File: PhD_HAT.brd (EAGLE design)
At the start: 62.2 x 64.4 mm, 31 parts, among them J1 USB_MINI-B_SMT, J2 AVR_SPI_PROG_3X2PTH, J3 PJ-102AH/BH, Q2 2.5A/30V/105mΩ, U1 ATMEGA328P-MUR, U2 FT231XS, U3 3.3V

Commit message: Checkin- version
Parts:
- removed C1: 0.1uF, SparkFun-Capacitors:0603
- removed R1, R2: 4.7k, SparkFun-Resistors:0603
- removed U$1: SPARKFUN-CONNECTORS_RIGHT_ANGLED_DC, AG54_E_series_v2.29:SPARKFUN-CONNECTORS_M8_RIGHT_ANGLE_CONN
- added SJ1, SJ2: (no value), Adafruit Crickit FeatherWing:MICROBUILDER_SOLDERJUMPER_REFLOW
- added U$2: RPI-ZERO, RPI-Zero:RASPBERRYPI_BASTELSTUBE_V13_RASPI_BOARD_B+_FULL
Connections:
- removed net SCL: R1.1, U$1.P$2, U1.28
- removed net SDA: R2.1, U$1.P$3, U1.27
- new net N$10: SJ1.2
- new net N$7: SJ1.1, U2.4
- new net N$8: SJ2.1, U2.20
- net 3.3V: no longer C1.1, R1.2, R2.2, U$1.P$1
- net GND: no longer C1.2, U$1.P$4
- net RX: now also SJ2.2; no longer U2.20
- net TX: no longer U2.4
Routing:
- net SDA: track 59.2 -> 0.00 mm, vias 1 -> 0
- net 3.3V: track 102.5 -> 56.1 mm, vias 6 -> 5
- net SCL: track 26.5 -> 0.00 mm
- net RX: track 65.4 -> 56.6 mm

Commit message: Check-in of design files
A partial check-in to switch laptops
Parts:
- removed H1, H2, H3, H4: MOUNT-HOLE3.0, holes:3,0
- removed U$2: RPI-ZERO, RPI-Zero:RASPBERRYPI_BASTELSTUBE_V13_RASPI_BOARD_B+_FULL
- added C1: 1.0uF, SparkFun-Capacitors:0603
- added C9: 10uF, SparkFun-Capacitors:EIA3216
- added J4: (no value), SparkFun-Connectors:SCREWTERMINAL-3.5MM-5
- added J5: (no value), SparkFun-Connectors:SCREWTERMINAL-3.5MM-2
- added J6: (no value), SparkFun-Connectors:SCREWTERMINAL-3.5MM-4
- added SJ3, SJ4: (no value), Adafruit Crickit FeatherWing:MICROBUILDER_SOLDERJUMPER_ARROW_NOPASTE
- added U4: MIC39100-5.0WS, MIC39100-5.0WS:SOT223
- added X1: RASPI_BOARD_B+_H, raspberrypi_bastelstube_v13:RASPI_BOARD_B+HAT
- moved J3 17.8 mm to (10.2, 14.0)
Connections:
- removed net N$10: SJ1.2
- new net 3V3: X1.1
- new net 5V: C9.+, J6.1, U4.3
- new net 5V0: X1.2
- new net CLOCK: J6.3, U1.10
- new net DATA: J6.4, U1.11
- new net LATCH: J6.2, U1.9
- new net N$11: SJ3.1, X1.8
- new net N$12: SJ4.1, X1.10
- net GND: now also C1.2, C9.-, J5.1, J5.2, U4.2, U4.TAB, X1.14, X1.17, X1.20, X1.25, X1.30, X1.34, X1.39, X1.4, X1.6, X1.9
- net RX: now also SJ3.2
- net TX: now also SJ1.2, SJ4.2
- net VIN: now also C1.1, J4.1, J4.2, J4.3, J4.4, J4.5, U4.1
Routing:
- net !RESET: track 62.9 -> 0.00 mm
- net RX: track 56.6 -> 0.00 mm, vias 2 -> 0
- net 3.3V: track 56.1 -> 0.00 mm, vias 5 -> 0
- net TX: track 50.5 -> 0.00 mm, vias 2 -> 0
- net V_USB: track 22.3 -> 0.00 mm, vias 2 -> 0
- net MOSI: track 15.2 -> 0.00 mm
- net SCK: track 13.4 -> 0.00 mm
- net GND: track 13.2 -> 0.00 mm, vias 1 -> 0
- net MISO: track 12.1 -> 0.00 mm
- net N$2: track 10.9 -> 0.00 mm, vias 2 -> 0
- net N$1: track 9.23 -> 0.00 mm
- net D-: track 7.74 -> 0.00 mm
- net D+: track 6.56 -> 0.00 mm
- net N$3: track 3.54 -> 0.00 mm
- net !DTR: track 2.80 -> 0.00 mm
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- removed copper zone on layer 16, net 3.3V
- removed copper zone on layer 1, net N$9
- removed copper zone on layer 1, net VIN
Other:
- board size 62.2 x 64.4 mm -> 65 x 56 mm
- board text added: "12V DC"
- board text removed: "09-11-2019"
- board text removed: "I2C Testing board"

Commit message: check -in
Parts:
- added C10: 10uF, SparkFun-Capacitors:EIA3216
- moved J6 99.0 mm to (29.1, 4.32)
- moved C1 79.7 mm to (20.4, 11.8)
- moved U4 78.4 mm to (21.9, 18.0)
- moved Q2 20.5 mm to (14.2, 14.0), turned to 90 degrees
- moved U3 18.7 mm to (15.5, 20.8)
- moved C7 15.9 mm to (12.6, 20.3)
- moved J4 2.44 mm to (3.96, 37.3)
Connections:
- net GND: now also C10.-
- net VIN: now also C10.+
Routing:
- removed copper zone on layer 1, net 3.3V

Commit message: Check-in
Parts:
- removed C4: 10nF, SparkFun-Capacitors:0603
- removed FB1: 30Ω/1.8A, SparkFun-Coils:0603
- moved SJ4 106.1 mm to (18.5, 45.8), turned to 270 degrees
- moved SJ2 105.4 mm to (46.4, 43.2), turned to 90 degrees
- moved SJ1 103.1 mm to (48.7, 43.2), turned to 90 degrees
- moved SJ3 102.0 mm to (15.9, 45.9), turned to 270 degrees
- moved J5 101.4 mm to (48.9, 4.22)
- moved C9 85.4 mm to (29.1, 11.1), turned to 270 degrees
- moved J1 37.1 mm to (60.4, 36.1), turned to 180 degrees
- moved C5 30.3 mm to (48.0, 29.2), turned to 270 degrees
- moved R4 27.6 mm to (52.3, 26.3), turned to 270 degrees
- moved S1 26.2 mm to (29.5, 44.9), turned to 180 degrees
- moved D2 25.6 mm to (52.0, 29.8), turned to 0 degrees
- moved R3 25.5 mm to (50.5, 26.3), turned to 270 degrees
- moved J2 24.4 mm to (39.4, 21.0), turned to 180 degrees
- moved D1 23.8 mm to (51.0, 29.8), turned to 0 degrees
- moved U2 21.8 mm to (49.2, 35.3), turned to 0 degrees
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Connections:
- removed net N$1: C4.2, FB1.2, J1.VBUS
- removed net V_USB: FB1.1, U2.15
- new net VBUS: J1.VBUS
- net 3.3V: now also U2.15
- net GND: no longer C4.1
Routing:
- net DATA: track 0.00 -> 34.1 mm
- net CLOCK: track 0.00 -> 30.8 mm
- net LATCH: track 0.00 -> 28.1 mm
- net 3.3V: track 0.00 -> 9.47 mm
- net GND: track 0.00 -> 5.06 mm
- added copper zone on layer 1, net 5V
- added copper zone on layer 1, net N$9
- added copper zone on layer 1, net VIN
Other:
- board text added: "CLK"
- board text added: "DAT"
- board text added: "LAT"
- board text added: "VIN"

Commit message: Update PhD_HAT.brd
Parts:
- moved SJ1 4.78 mm to (44.0, 43.2)
- moved C2 1.55 mm to (37.9, 34.0)
- moved C8 0.61 mm to (15.3, 24.3)
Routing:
- net N$2: track 0.00 -> 26.7 mm, vias 0 -> 2
- net SCK: track 0.00 -> 15.0 mm
- net 3.3V: track 9.47 -> 18.4 mm, vias 0 -> 6
- net D-: track 0.00 -> 8.72 mm
- net D+: track 0.00 -> 7.31 mm
- net N$8: track 0.00 -> 4.49 mm
- net !DTR: track 0.00 -> 2.60 mm
- net N$4: track 0.00 -> 2.11 mm
- net N$5: track 0.00 -> 2.04 mm
- net N$3: track 0.00 -> 2.04 mm
- net N$6: track 0.00 -> 2.01 mm
- added copper zone on layer 1, net 3.3V
- added copper zone on layer 16, net 3.3V

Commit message: completed board file
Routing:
- net !RESET: track 0.00 -> 68.6 mm, vias 0 -> 1
- net RX: track 0.00 -> 57.5 mm, vias 0 -> 3
- net TX: track 0.00 -> 47.3 mm
- net 3.3V: track 18.4 -> 64.3 mm, vias 6 -> 9
- net MOSI: track 0.00 -> 15.0 mm
- net MISO: track 0.00 -> 14.9 mm, vias 0 -> 1
- net N$7: track 0.00 -> 13.4 mm
- net N$12: track 0.00 -> 7.96 mm
- net N$11: track 0.00 -> 7.81 mm
- net GND: track 5.06 -> 6.70 mm, vias 0 -> 1
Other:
- board text added: "12V"
- board text added: "FTDI JUMPER"
- board text added: "GND"
- board text added: "October 2019"
- board text added: "Personal Health Dashboard"
- board text added: "RPi JUMPER"
- board text removed: "VIN"

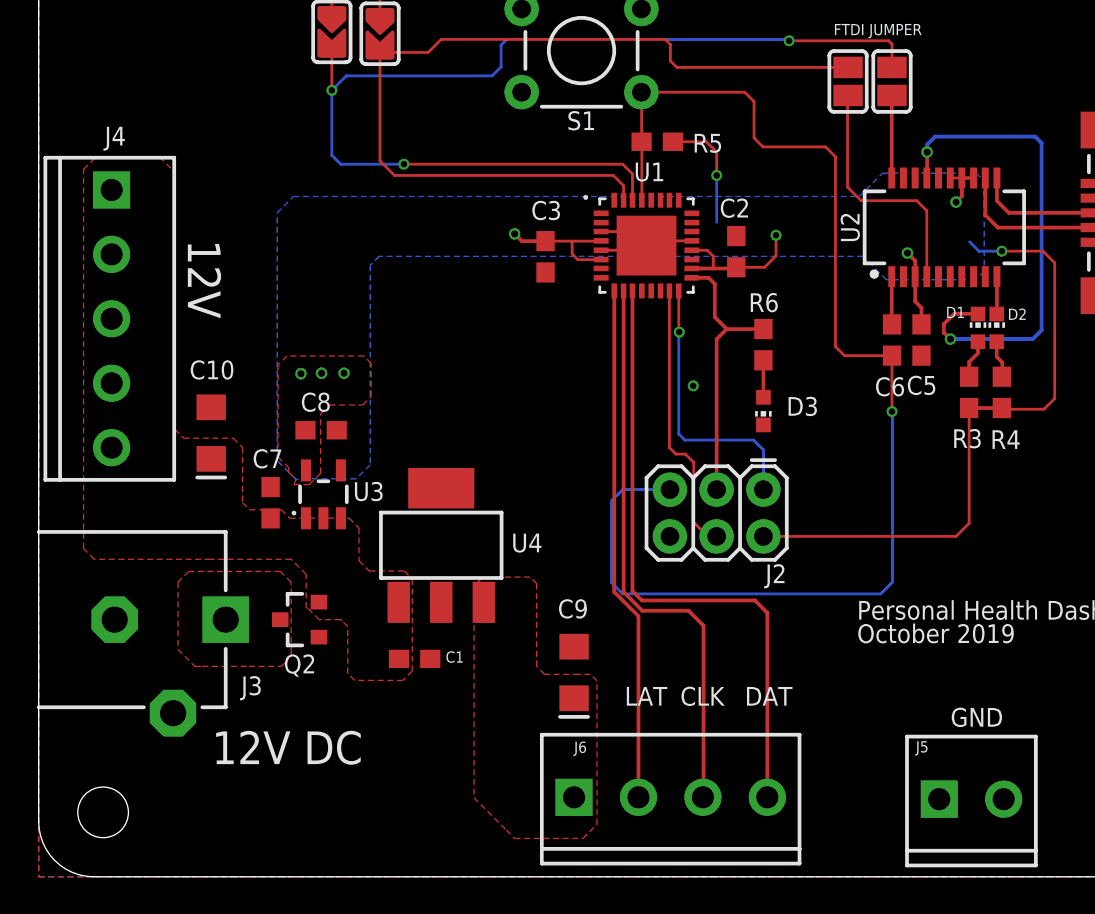
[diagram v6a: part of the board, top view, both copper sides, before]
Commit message: Change of power flow sequence
The max input voltage for the 3.3V regulator is 6V. The design was originally designed to receive 12V. This smoked the regulator. Changed the design to receive input from a 5V regulator.
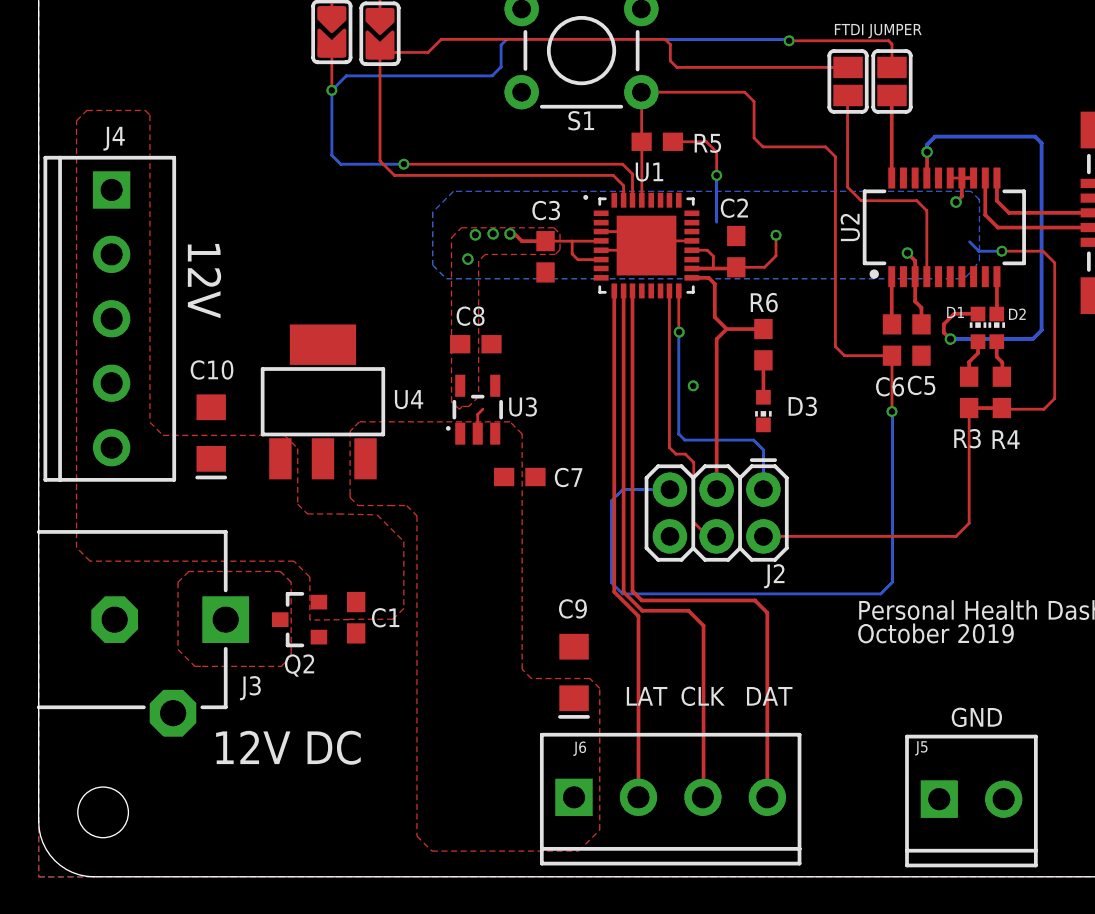
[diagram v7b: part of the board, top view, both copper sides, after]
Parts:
- moved C7 13.6 mm to (26.1, 21.7), turned to 0 degrees
- moved U4 10.1 mm to (15.4, 25.8)
- moved C8 9.62 mm to (23.7, 28.9)
- moved U3 9.56 mm to (23.9, 25.4)
- moved C1 3.88 mm to (17.2, 14.1), turned to 270 degrees
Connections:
- net 5V: now also C7.1, U3.1, U3.3
- net VIN: no longer C7.1, U3.1, U3.3
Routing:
- net GND: track 6.70 -> 8.14 mm
